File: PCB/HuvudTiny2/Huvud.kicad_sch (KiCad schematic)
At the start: 107 parts, among them J1 MOLEX Micro Fit 2x2, J10 FAN0, J2 DBG, J3 THERM, J4 FAN1, J5 FAN2, J6 Heater, J7 Endstop, J8 THERM, J9 STEPPER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

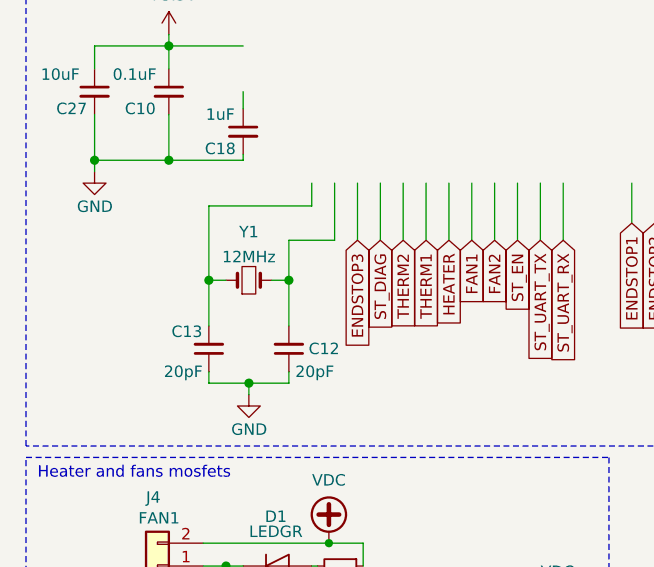
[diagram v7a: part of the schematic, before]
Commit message: Add SPI flash symbol.
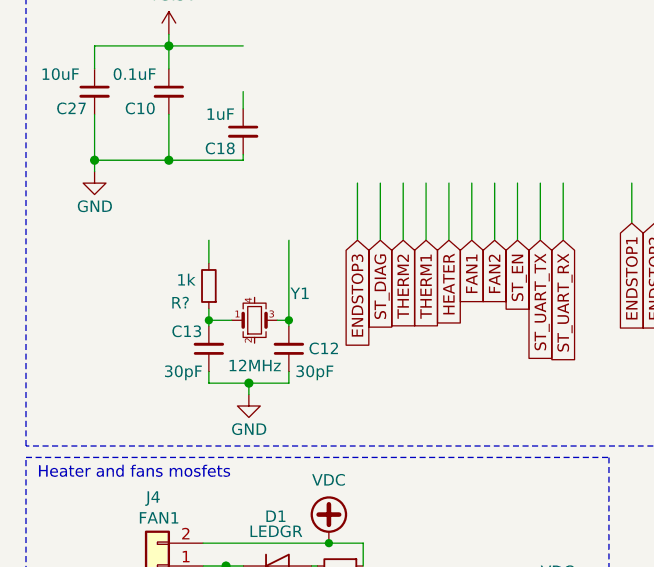
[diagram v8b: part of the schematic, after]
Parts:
- removed Y1: 12MHz, Crystal:Crystal_SMD_3225-4Pin_3.2x2.5mm, symbol Device:Crystal_Small
- added R?: 1k, Resistor_SMD:R_0402_1005Metric, symbol Device:R_Small
- added Y1: 12MHz, Crystal:Crystal_SMD_3225-4Pin_3.2x2.5mm, symbol Device:Crystal_GND24_Small
- C12, C13: value 20pF -> 30pF; LCSC C1554 -> C1570
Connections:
- net at C12.2: now also Y1.3
- net at C13.2: now also R?.1, Y1.1
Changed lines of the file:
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@@
   (junction (at 249.555 122.555) (diameter 1.016) (color 0 0 0 0)
   )
+  (junction (at 41.91 87.63) (diameter 0) (color 0 0 0 0)
+  )
   (junction (at 253.365 122.555) (diameter 1.016) (color 0 0 0 0)
   )
@@
   (junction (at 120.65 74.295) (diameter 1.016) (color 0 0 0 0)
   )
-  (junction (at 234.95 106.68) (diameter 1.016) (color 0 0 0 0)
+  (junction (at 33.02 87.63) (diameter 0) (color 0 0 0 0)
   )
-  (junction (at 41.91 83.185) (diameter 1.016) (color 0 0 0 0)
+  (junction (at 234.95 106.68) (diameter 1.016) (color 0 0 0 0)
   )
   (junction (at 273.685 40.64) (diameter 1.016) (color 0 0 0 0)
   )
-  (junction (at 33.02 83.185) (diameter 1.016) (color 0 0 0 0)
-  )
   (junction (at 28.575 69.85) (diameter 1.016) (color 0 0 0 0)
   )
@@
     (stroke (width 0) (type solid))
   )
-  (wire (pts (xy 33.02 83.185) (xy 34.925 83.185))
-    (stroke (width 0) (type solid))
-  )
   (wire (pts (xy 279.4 35.56) (xy 279.4 55.88))
     (stroke (width 0) (type solid))
@@
     (stroke (width 0) (type solid))
   )
-  (wire (pts (xy 41.91 83.185) (xy 41.91 88.265))
-    (stroke (width 0) (type solid))
-  )
-  (wire (pts (xy 46.99 72.39) (xy 46.99 78.74))
+  (wire (pts (xy 41.91 78.74) (xy 41.91 87.63))
     (stroke (width 0) (type solid))
   )
@@
     (stroke (width 0) (type solid))
   )
-  (wire (pts (xy 33.02 74.93) (xy 33.02 83.185))
-    (stroke (width 0) (type solid))
-  )
-  (wire (pts (xy 44.45 72.39) (xy 44.45 74.93))
-    (stroke (width 0) (type solid))
-  )
-  (wire (pts (xy 44.45 74.93) (xy 33.02 74.93))
-    (stroke (width 0) (type solid))
-  )
   (wire (pts (xy 164.465 134.62) (xy 164.465 133.35))
     (stroke (width 0) (type solid))
@@
     (stroke (width 0) (type solid))
   )
-  (wire (pts (xy 40.005 83.185) (xy 41.91 83.185))
-    (stroke (width 0) (type solid))
-  )
   (wire (pts (xy 166.37 30.48) (xy 181.61 30.48))
     (stroke (width 0) (type solid))
@@
     (stroke (width 0) (type solid))
   )
+  (wire (pts (xy 33.02 78.74) (xy 33.02 81.28))
+    (stroke (width 0) (type default))
+  )
   (wire (pts (xy 101.6 150.495) (xy 106.68 150.495))
     (stroke (width 0) (type default))
@@
     (stroke (width 0) (type solid))
   )
-  (wire (pts (xy 41.91 78.74) (xy 41.91 83.185))
-    (stroke (width 0) (type solid))
-  )
-  (wire (pts (xy 46.99 78.74) (xy 41.91 78.74))
-    (stroke (width 0) (type solid))
-  )
   (wire (pts (xy 69.85 125.095) (xy 70.485 125.095))
     (stroke (width 0) (type solid))
@@
     (stroke (width 0) (type dash))
   )
+  (wire (pts (xy 33.02 86.36) (xy 33.02 87.63))
+    (stroke (width 0) (type default))
+  )
   (wire (pts (xy 245.11 151.13) (xy 245.11 152.4))
     (stroke (width 0) (type default))
@@
     (stroke (width 0) (type solid))
   )
+  (wire (pts (xy 33.02 87.63) (xy 33.02 88.265))
+    (stroke (width 0) (type solid))
+  )
   (wire (pts (xy 130.175 173.355) (xy 130.175 176.53))
     (stroke (width 0) (type default))
@@
     (stroke (width 0) (type dash))
   )
+  (wire (pts (xy 41.91 87.63) (xy 41.91 88.265))
+    (stroke (width 0) (type solid))
+  )
   (wire (pts (xy 93.345 150.495) (xy 93.345 155.575))
     (stroke (width 0) (type default))
@@
     (stroke (width 0) (type solid))
   )
-  (wire (pts (xy 33.02 83.185) (xy 33.02 88.265))
-    (stroke (width 0) (type solid))
+  (wire (pts (xy 40.64 87.63) (xy 41.91 87.63))
+    (stroke (width 0) (type default))
   )
   (wire (pts (xy 205.74 144.78) (xy 205.74 143.51))
@@
     (stroke (width 0) (type default))
   )
+  (wire (pts (xy 33.02 87.63) (xy 35.56 87.63))
+    (stroke (width 0) (type default))
+  )
   (text "Voltage Regulators" (at 191.77 134.62 0)
     (effects (font (size 1.27 1.27)) (justify left bottom))
@@
       (effects (font (size 1.27 1.27)))
     )
-    (property "Value" "20pF" (id 1) (at 44.7802 93.345 0)
+    (property "Value" "30pF" (id 1) (at 44.7802 93.345 0)
       (effects (font (size 1.27 1.27)))
     )
@@
       (effects (font (size 1.27 1.27)) hide)
     )
-    (property "LCSC" "C1554" (id 4) (at 41.91 90.805 90)
+    (property "LCSC" "C1570" (id 4) (at 41.91 90.805 90)
       (effects (font (size 1.27 1.27)) hide)
     )
@@
       (effects (font (size 1.27 1.27)))
     )
-    (property "Value" "20pF" (id 1) (at 30.1752 93.345 0)
+    (property "Value" "30pF" (id 1) (at 30.1752 93.345 0)
       (effects (font (size 1.27 1.27)))
     )
@@
       (effects (font (size 1.27 1.27)) hide)
     )
-    (property "LCSC" "C1554" (id 4) (at 33.02 90.805 0)
+    (property "LCSC" "C1570" (id 4) (at 33.02 90.805 0)
       (effects (font (size 1.27 1.27)) hide)
     )
@@
     (pin "3")
   )
-  (symbol (lib_id "Device:Crystal_Small") (at 37.465 83.185 0) (unit 1)
-    (in_bom yes) (on_board yes) (fields_autoplaced)
-    (property "Reference" "Y1" (id 0) (at 37.465 77.8214 0)
-      (effects (font (size 1.27 1.27)))
-    )
-    (property "Value" "12MHz" (id 1) (at 37.465 80.5965 0)
-      (effects (font (size 1.27 1.27)))
-    )
-    (property "Footprint" "Crystal:Crystal_SMD_3225-4Pin_3.2x2.5mm" (id 2) (at 37.465 83.185 0)
-      (effects (font (size 1.27 1.27)) hide)
-    )
-    (property "Datasheet" "~" (id 3) (at 37.465 83.185 0)
-      (effects (font (size 1.27 1.27)) hide)
-    )
-    (property "LCSC" "C9002" (id 4) (at 37.465 83.185 0)
-      (effects (font (size 1.27 1.27)) hide)
-    )
-    (pin "1")
-    (pin "2")
-  )
   (symbol (lib_id "Connector_Generic:Conn_01x02") (at 27.305 147.32 180) (unit 1)
     (in_bom yes) (on_board yes)
@@
     (pin "2")
   )
+  (symbol (lib_id "Device:R_Small") (at 33.02 83.82 180) (unit 1)
+    (in_bom yes) (on_board yes)
+    (property "Reference" "R?" (id 0) (at 29.845 85.725 0)
+      (effects (font (size 1.27 1.27)))
+    )
+    (property "Value" "1k" (id 1) (at 30.48 83.185 0)
+      (effects (font (size 1.27 1.27)))
+    )
+    (property "Footprint" "Resistor_SMD:R_0402_1005Metric" (id 2) (at 33.02 83.82 0)
+      (effects (font (size 1.27 1.27)) hide)
+    )
+    (property "Datasheet" "~" (id 3) (at 33.02 83.82 0)
+      (effects (font (size 1.27 1.27)) hide)
+    )
+    (property "LCSC" "C11702" (id 4) (at 33.02 83.82 90)
+      (effects (font (size 1.27 1.27)) hide)
+    )
+    (pin "1")
+    (pin "2")
+  )
   (symbol (lib_id "Diode:BAT54S") (at 111.76 150.495 270) (mirror x) (unit 1)
     (in_bom yes) (on_board yes)
@@
     (pin "2")
   )
+  (symbol (lib_id "Device:Crystal_GND24_Small") (at 38.1 87.63 0) (unit 1)
+    (in_bom yes) (on_board yes)
+    (property "Reference" "Y1" (id 0) (at 43.18 84.6837 0)
+      (effects (font (size 1.27 1.27)))
+    )
+    (property "Value" "12MHz" (id 1) (at 38.1 92.71 0)
+      (effects (font (size 1.27 1.27)))
+    )
+    (property "Footprint" "Crystal:Crystal_SMD_3225-4Pin_3.2x2.5mm" (id 2) (at 38.1 87.63 0)
+      (effects (font (size 1.27 1.27)) hide)
+    )
+    (property "Datasheet" "~" (id 3) (at 38.1 87.63 0)
+      (effects (font (size 1.27 1.27)) hide)
+    )
+    (property "LCSC" "C9002" (id 4) (at 38.1 87.63 0)
+      (effects (font (size 1.27 1.27)) hide)
+    )
+    (pin "1")
+    (pin "2")
+    (pin "3")
+    (pin "4")
+  )
   (symbol (lib_id "Device:R_Small") (at 97.79 150.495 270) (unit 1)
     (in_bom yes) (on_board yes)
@@
     )
     (path "/00000000-0000-0000-0000-00005efceeb6"
-      (reference "C12") (unit 1) (value "20pF") (footprint "Capacitor_SMD:C_0402_1005Metric")
+      (reference "C12") (unit 1) (value "30pF") (footprint "Capacitor_SMD:C_0402_1005Metric")
     )
     (path "/00000000-0000-0000-0000-00005efdcd85"
-      (reference "C13") (unit 1) (value "20pF") (footprint "Capacitor_SMD:C_0402_1005Metric")
+      (reference "C13") (unit 1) (value "30pF") (footprint "Capacitor_SMD:C_0402_1005Metric")
     )
     (path "/2e4bc6b2-d2a2-4949-beab-bd27c27a1b11"
@@
       (reference "R43") (unit 1) (value "10k") (footprint "Resistor_SMD:R_0402_1005Metric")
     )
+    (path "/5f8a4405-b12f-46df-b275-80a1691dd4b0"
+      (reference "R?") (unit 1) (value "1k") (footprint "Resistor_SMD:R_0402_1005Metric")
+    )
     (path "/a1557e14-8e6d-4050-8f05-66ab36354756"
       (reference "SW1") (unit 1) (value "SW_Push") (footprint "Button_Switch_SMD:SW_SPST_EVQP2")
@@
       (reference "U5") (unit 1) (value "XC6206PxxxMR") (footprint "Package_TO_SOT_SMD:SOT-23")
     )
-    (path "/09ab032e-04b3-4b4a-954a-4fc1a8e77640"
+    (path "/826a22b3-cf90-4ca6-806d-060835b51dd9"
       (reference "Y1") (unit 1) (value "12MHz") (footprint "Crystal:Crystal_SMD_3225-4Pin_3.2x2.5mm")
     )
